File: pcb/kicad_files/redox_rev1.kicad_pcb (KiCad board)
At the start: 2 copper layers, 162.2 x 126.5 mm, 79 parts, among them J1 OLED-Lily58-cache, K0 KEYSW, K1 KEYSW, K10 KEYSW, K11 KEYSW, K12 KEYSW, K13 KEYSW, K14 KEYSW, K15 KEYSW, K2 KEYSW, K20 KEYSW, K21 KEYSW, K22 KEYSW, K23 KEYSW, K24 KEYSW, K25 KEYSW, K26 KEYSW, K3 KEYSW, K30 KEYSW, K31 KEYSW, K32 KEYSW, K33 KEYSW, K34 KEYSW, K35 KEYSW, K36 KEYSW, K4 KEYSW, K40 KEYSW, K41 KEYSW, K42 KEYSW, K43 KEYSW, K44 KEYSW, K45 KEYSW, K46 KEYSW, K5 KEYSW, U1 ProMicro

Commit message: Added pika :)
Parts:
- added G***: LOGO, keyswitches:school_logo, B.Cu at (208.2, 82.1)
- added G***: LOGO, keyswitches:school_logo, F.Cu at (208.2, 82.1)
- added G***: LOGO, keyswitches:pika, B.Cu at (159.8, 103.6)
- added G***: LOGO, keyswitches:pika_reflected, F.Cu at (159.6, 103.6)

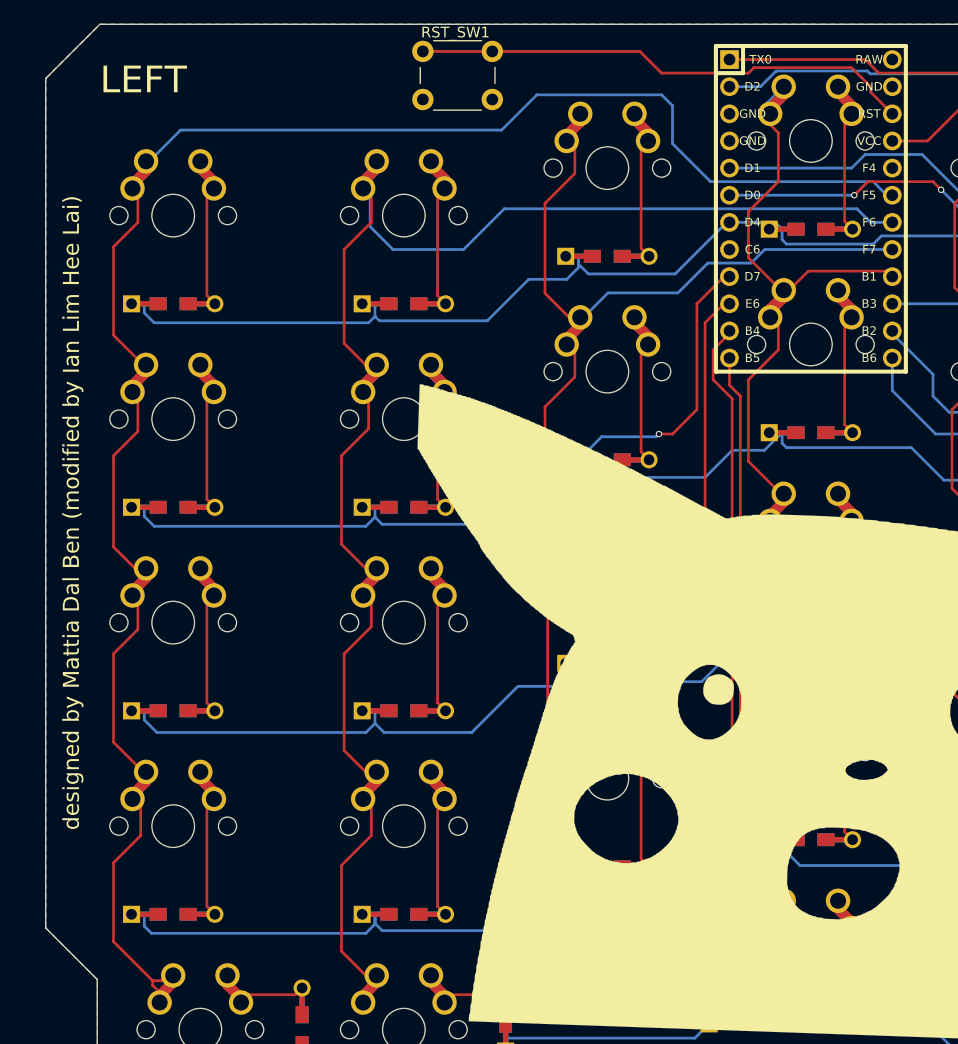
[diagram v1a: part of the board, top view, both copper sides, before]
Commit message: shifted keys to 1.5u
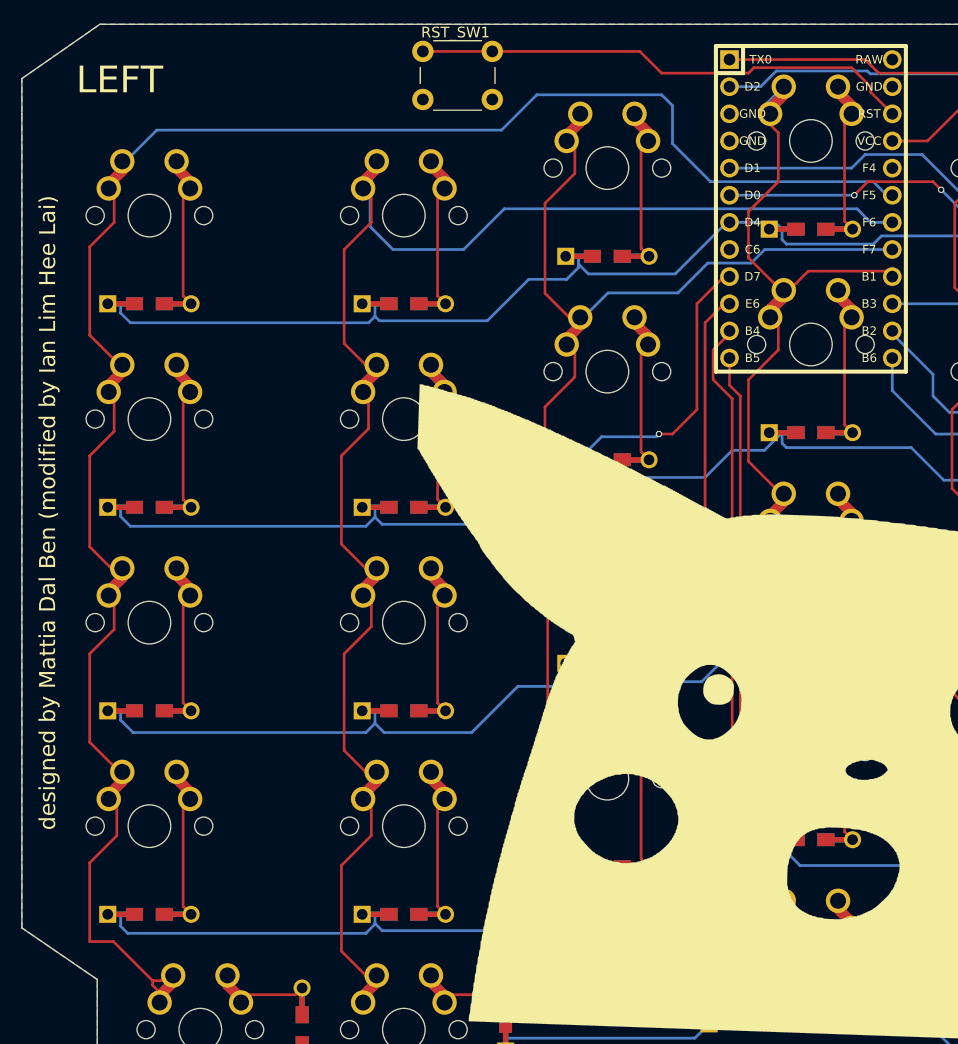
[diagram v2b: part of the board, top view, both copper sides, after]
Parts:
- moved D0 2.22 mm to (89.2, 74.9)
- moved D10 2.22 mm to (89.2, 94.0)
- moved D20 2.22 mm to (89.2, 113.0)
- moved D30 2.22 mm to (89.2, 132.1)
- moved K0 2.22 mm to (89.2, 66.7)
- moved K10 2.22 mm to (89.2, 85.7)
- moved K20 2.22 mm to (89.2, 104.8)
- moved K30 2.22 mm to (89.2, 123.8)
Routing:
- net col0: track 183.1 -> 187.6 mm
- net row2: track 188.9 -> 191.2 mm
- net row0: track 112.0 -> 114.2 mm
- net row1: track 142.1 -> 144.3 mm
- net row3: track 207.9 -> 208.6 mm
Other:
- board size 162.2 x 126.5 mm -> 164.4 x 126.5 mm
